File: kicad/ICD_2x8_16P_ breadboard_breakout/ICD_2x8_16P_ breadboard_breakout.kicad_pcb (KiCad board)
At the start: 2 copper layers, 28 x 30.5 mm, 3 parts, among them J1 Conn_02x08_Top_Bottom, J2 Conn_01x08, J3 Conn_01x08

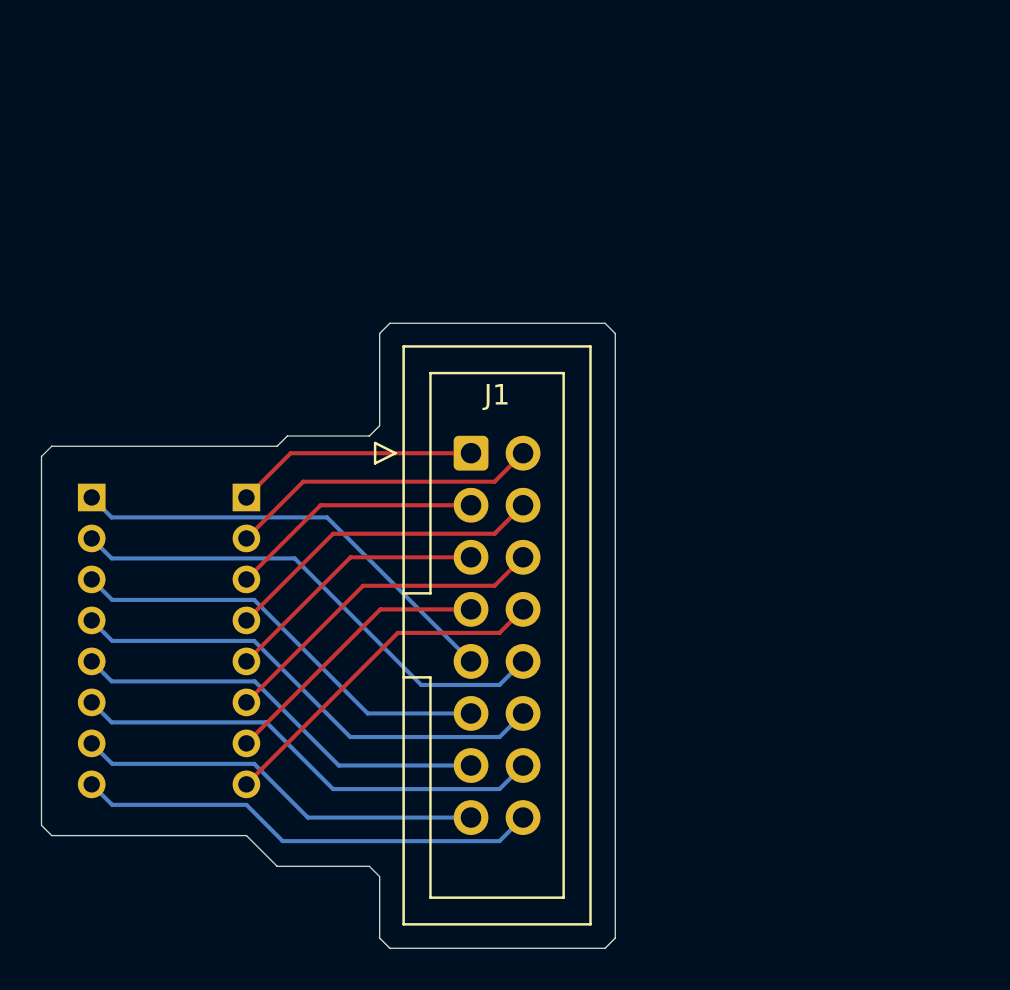
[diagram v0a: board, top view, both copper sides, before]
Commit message: Major progress on Serial, KiCAD models, and Python libraries for sensor module base.
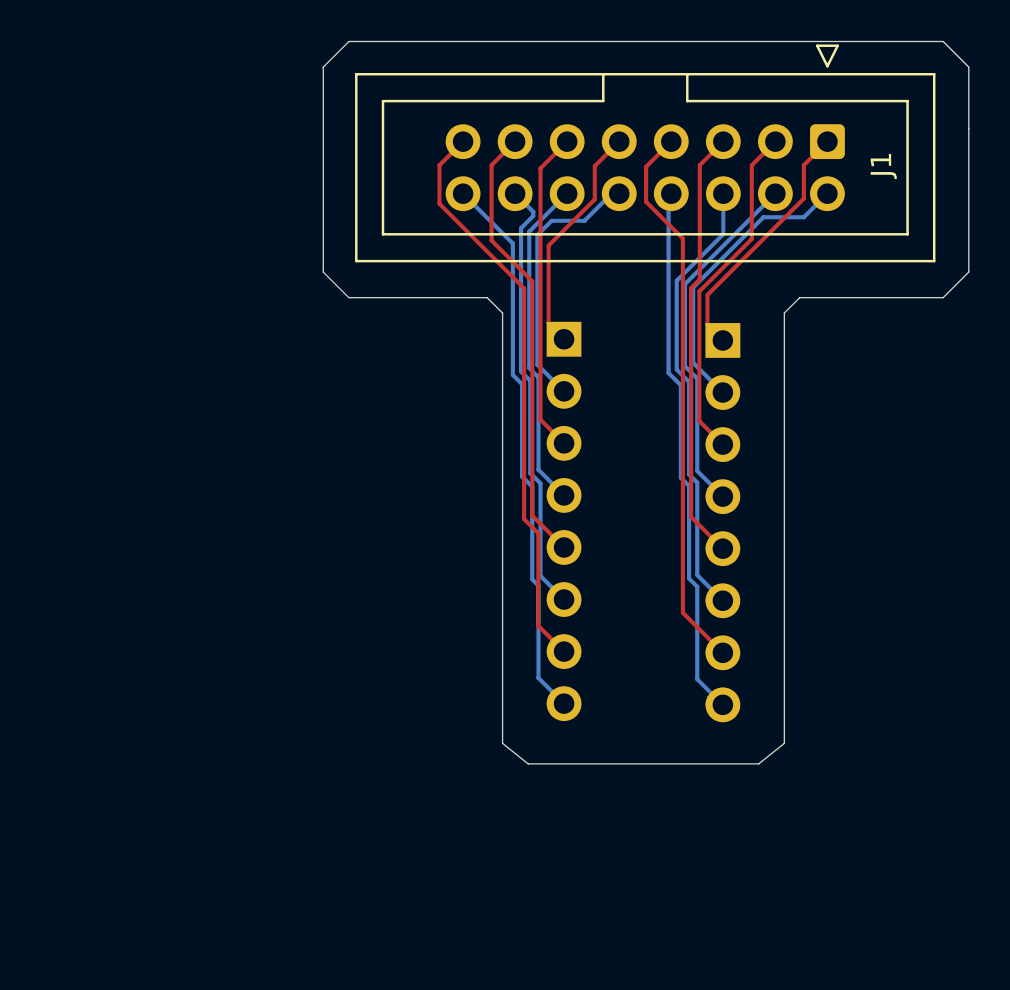
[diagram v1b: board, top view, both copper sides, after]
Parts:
- J2, J3: footprint Connector_PinHeader_2.00mm:PinHeader_1x08_P2.00mm_Vertical -> Connector_PinHeader_2.54mm:PinHeader_1x08_P2.54mm_Vertical
- moved J2 24.5 mm to (116.2, 55.3)
- moved J3 24.3 mm to (108.5, 55.3)
- moved J1 23.1 mm to (121.4, 45.6), turned to -90 degrees
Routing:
- net Net-(J1-Pin_7): track 13.7 -> 27.0 mm
- net Net-(J1-Pin_10): track 24.5 -> 13.0 mm
- net Net-(J1-Pin_9): track 21.8 -> 11.4 mm
- net Net-(J1-Pin_8): track 17.0 -> 26.1 mm
- net Net-(J1-Pin_5): track 13.1 -> 21.2 mm
- net Net-(J1-Pin_15): track 20.0 -> 27.9 mm
- net Net-(J1-Pin_12): track 23.9 -> 16.2 mm
- net Net-(J1-Pin_11): track 21.2 -> 15.7 mm
- net Net-(J1-Pin_6): track 16.4 -> 21.7 mm
- net Net-(J1-Pin_3): track 12.5 -> 16.8 mm
- net Net-(J1-Pin_16): track 22.7 -> 26.9 mm
- net Net-(J1-Pin_14): track 23.3 -> 21.3 mm
- net Net-(J1-Pin_4): track 15.8 -> 17.4 mm
- net Net-(J1-Pin_13): track 20.6 -> 21.7 mm
- net Net-(J1-Pin_2): track 15.2 -> 14.2 mm
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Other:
- board size 28 x 30.5 mm -> 31.5 x 35.2 mm
